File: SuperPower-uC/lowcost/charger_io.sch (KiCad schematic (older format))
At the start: 13 parts, among them J3 USB_C_Receptacle_USB2.0, J4 Solar in, Q3 S8050, Q4 S8050, U5 CH340G, U6 AMS1117-3.3, Y1 12MHZ

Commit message: updated with kicad v5.1.7
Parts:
- J3: footprint Connector_USB:USB_C_Receptacle_XKB_U262-16XN-4BVC11 -> (none)
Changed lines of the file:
@@
 	5250 2900 5250 3100
 Connection ~ 5250 2900
-Connection ~ 4700 3150
 Wire Wire Line
 	4700 3150 4900 3150
 Wire Wire Line
 	4700 3250 4700 3150
-Connection ~ 4700 3450
 Wire Wire Line
 	4700 3450 4700 3350
 Wire Wire Line
 	4700 3450 5000 3450
-$Comp
-L Connector:USB_C_Receptacle_USB2.0 J3
-U 1 1 5F7DCB22
-P 4100 3250
-F 0 "J3" H 4207 4117 50  0000 C CNN
-F 1 "USB_C_Receptacle_USB2.0" H 4207 4026 50  0000 C CNN
-F 2 "Connector_USB:USB_C_Receptacle_XKB_U262-16XN-4BVC11" H 4250 3250 50  0001 C CNN
-F 3 "https://datasheet.lcsc.com/szlcsc/2002271811_XKB-Connectivity-U262-161N-4BVC11_C319148.pdf" H 4250 3250 50  0001 C CNN
-	1    4100 3250
-	1    0    0    -1
-$EndComp
 Wire Wire Line
 	6350 2600 6350 2750
@@
 Text HLabel 6700 2600 2    50   Output ~ 0
 VCHARGE
+$Comp
+L Connector:USB_C_Receptacle_USB2.0 J3
+U 1 1 5F80E438
+P 4100 3250
+F 0 "J3" H 4207 4117 50  0000 C CNN
+F 1 "USB_C_Receptacle_USB2.0" H 4207 4026 50  0000 C CNN
+F 2 "" H 4250 3250 50  0001 C CNN
+F 3 "https://www.usb.org/sites/default/files/documents/usb_type-c.zip" H 4250 3250 50  0001 C CNN
+	1    4100 3250
+	1    0    0    -1
+$EndComp
+Connection ~ 4700 3150
+Connection ~ 4700 3450
 $EndSCHEMATC

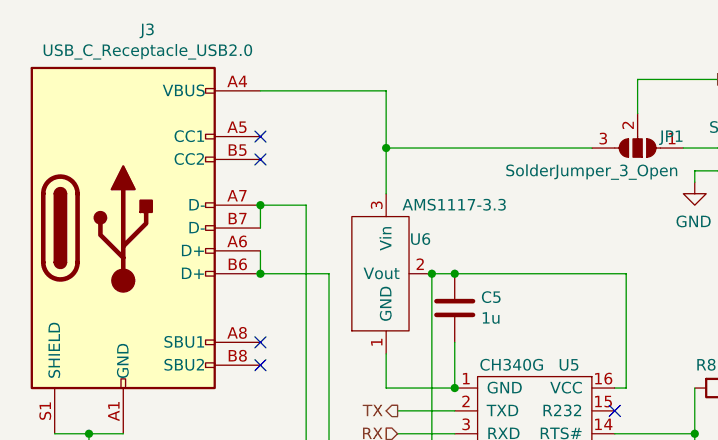
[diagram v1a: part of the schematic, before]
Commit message: added usb cc pin pulldowns and deleted cache
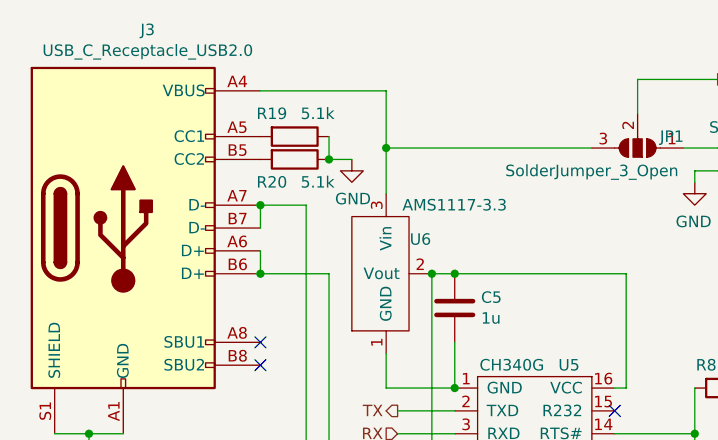
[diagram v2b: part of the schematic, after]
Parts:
- added R19, R20: 5.1k, Resistor_SMD:R_0603_1608Metric_Pad1.05x0.95mm_HandSolder, symbol Device:R
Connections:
- net GND: now also R19.1, R20.1
- net at J3.A5 (CC1): now also R19.2
- net at J3.B5 (CC2): now also R20.2
- no-connect marks 9 -> 7
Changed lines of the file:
@@
 NoConn ~ 4700 3750
 NoConn ~ 4700 3850
-NoConn ~ 4700 2950
-NoConn ~ 4700 2850
 Wire Wire Line
 	5250 2900 5250 3100
@@
 Connection ~ 4700 3150
 Connection ~ 4700 3450
+$Comp
+L Device:R R19
+U 1 1 5F81A493
+P 4850 2850
+F 0 "R19" V 4750 2750 50  0000 C CNN
+F 1 "5.1k" V 4750 2950 50  0000 C CNN
+F 2 "Resistor_SMD:R_0603_1608Metric_Pad1.05x0.95mm_HandSolder" V 4780 2850 50  0001 C CNN
+F 3 "~" H 4850 2850 50  0001 C CNN
+F 4 "C23186" V 4850 2850 50  0001 C CNN "LCSC"
+	1    4850 2850
+	0    1    1    0
+$EndComp
+$Comp
+L Device:R R20
+U 1 1 5F81C386
+P 4850 2950
+F 0 "R20" V 4950 2850 50  0000 C CNN
+F 1 "5.1k" V 4950 3050 50  0000 C CNN
+F 2 "Resistor_SMD:R_0603_1608Metric_Pad1.05x0.95mm_HandSolder" V 4780 2950 50  0001 C CNN
+F 3 "~" H 4850 2950 50  0001 C CNN
+F 4 "C23186" V 4850 2950 50  0001 C CNN "LCSC"
+	1    4850 2950
+	0    1    1    0
+$EndComp
+Wire Wire Line
+	5000 2850 5000 2950
+$Comp
+L power:GND #PWR?
+U 1 1 5F820F01
+P 5100 2950
+F 0 "#PWR?" H 5100 2700 50  0001 C CNN
+F 1 "GND" H 5105 2777 50  0000 C CNN
+F 2 "" H 5100 2950 50  0001 C CNN
+F 3 "" H 5100 2950 50  0001 C CNN
+	1    5100 2950
+	1    0    0    -1
+$EndComp
+Wire Wire Line
+	5100 2950 5000 2950
+Connection ~ 5000 2950
 $EndSCHEMATC

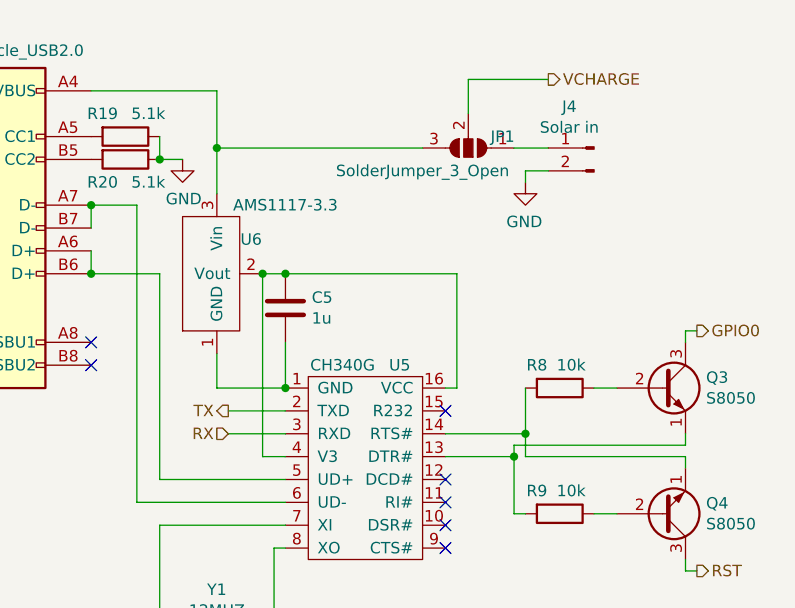
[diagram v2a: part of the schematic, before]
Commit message: fixed erc errors
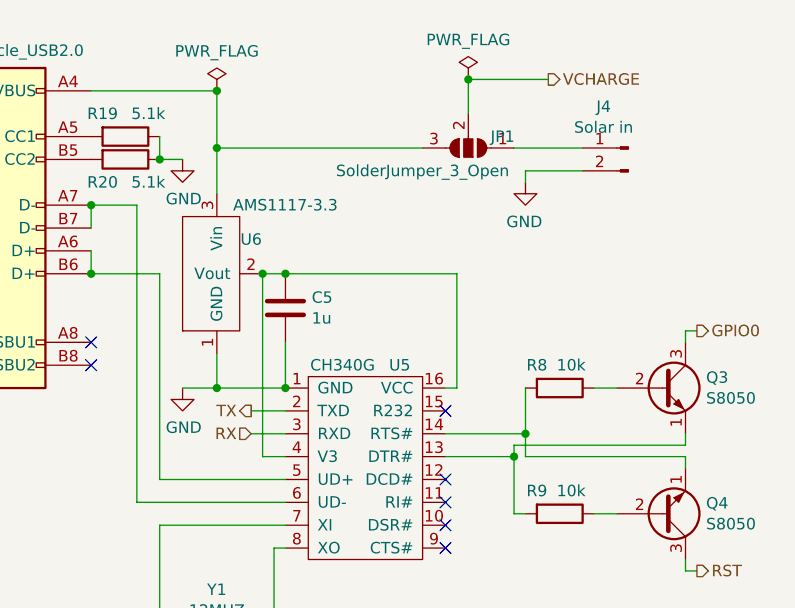
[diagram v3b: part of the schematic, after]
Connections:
- net GND: now also C5.2, U5.1 (GND), U6.1 (GND)
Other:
- moved on the sheet: J4
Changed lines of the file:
@@
 Wire Wire Line
 	5250 2900 6150 2900
-Wire Wire Line
-	6700 2900 6550 2900
 Connection ~ 5000 5100
 Wire Wire Line
@@
 	6600 3000 6600 3050
 Wire Wire Line
-	6700 3000 6600 3000
+	6850 3000 6600 3000
 $Comp
 L power:GND #PWR0123
@@
 $EndComp
 Wire Wire Line
-	5300 4150 5550 4150
-Wire Wire Line
-	5300 4050 5550 4050
+	5400 4150 5550 4150
+Wire Wire Line
+	5400 4050 5550 4050
 Connection ~ 5550 3950
 Wire Wire Line
@@
 L Connector:Conn_01x02_Male J4
 U 1 1 5F7CE401
-P 6900 2900
-F 0 "J4" H 7008 3081 50  0000 C CNN
-F 1 "Solar in" H 7008 2990 50  0000 C CNN
-F 2 "Connector_JST:JST_EH_S2B-EH_1x02_P2.50mm_Horizontal" H 6900 2900 50  0001 C CNN
-F 3 "https://datasheet.lcsc.com/szlcsc/1811051822_JST-Sales-America-S2B-XH-A-LF-SN_C157931.pdf" H 6900 2900 50  0001 C CNN
-F 4 "C157931" H 6900 2900 50  0001 C CNN "LCSC"
-	1    6900 2900
+P 7050 2900
+F 0 "J4" H 7158 3081 50  0000 C CNN
+F 1 "Solar in" H 7158 2990 50  0000 C CNN
+F 2 "Connector_JST:JST_EH_S2B-EH_1x02_P2.50mm_Horizontal" H 7050 2900 50  0001 C CNN
+F 3 "https://datasheet.lcsc.com/szlcsc/1811051822_JST-Sales-America-S2B-XH-A-LF-SN_C157931.pdf" H 7050 2900 50  0001 C CNN
+F 4 "C157931" H 7050 2900 50  0001 C CNN "LCSC"
+	1    7050 2900
 	-1   0    0    -1
 $EndComp
@@
 	1    0    0    -1
 $EndComp
-Text HLabel 5300 4150 0    50   Input ~ 0
+Text HLabel 5400 4150 0    50   Input ~ 0
 RX
-Text HLabel 5300 4050 0    50   Output ~ 0
+Text HLabel 5400 4050 0    50   Output ~ 0
 TX
 Text HLabel 6700 2600 2    50   Output ~ 0
@@
 	5000 2850 5000 2950
 $Comp
-L power:GND #PWR?
+L power:GND #PWR0124
 U 1 1 5F820F01
 P 5100 2950
-F 0 "#PWR?" H 5100 2700 50  0001 C CNN
+F 0 "#PWR0124" H 5100 2700 50  0001 C CNN
 F 1 "GND" H 5105 2777 50  0000 C CNN
 F 2 "" H 5100 2950 50  0001 C CNN
@@
 	5100 2950 5000 2950
 Connection ~ 5000 2950
+$Comp
+L power:GND #PWR0125
+U 1 1 5F8616D9
+P 5100 3950
+F 0 "#PWR0125" H 5100 3700 50  0001 C CNN
+F 1 "GND" H 5105 3777 50  0000 C CNN
+F 2 "" H 5100 3950 50  0001 C CNN
+F 3 "" H 5100 3950 50  0001 C CNN
+	1    5100 3950
+	1    0    0    -1
+$EndComp
+Wire Wire Line
+	5100 3950 5250 3950
+Connection ~ 5250 3950
+$Comp
+L power:PWR_FLAG #FLG0101
+U 1 1 5F872CCA
+P 5250 2650
+F 0 "#FLG0101" H 5250 2725 50  0001 C CNN
+F 1 "PWR_FLAG" H 5250 2823 50  0000 C CNN
+F 2 "" H 5250 2650 50  0001 C CNN
+F 3 "~" H 5250 2650 50  0001 C CNN
+	1    5250 2650
+	1    0    0    -1
+$EndComp
+Connection ~ 5250 2650
+$Comp
+L power:PWR_FLAG #FLG0104
+U 1 1 5F8735A3
+P 6350 2600
+F 0 "#FLG0104" H 6350 2675 50  0001 C CNN
+F 1 "PWR_FLAG" H 6350 2773 50  0000 C CNN
+F 2 "" H 6350 2600 50  0001 C CNN
+F 3 "~" H 6350 2600 50  0001 C CNN
+	1    6350 2600
+	1    0    0    -1
+$EndComp
+Connection ~ 6350 2600
+Wire Wire Line
+	6550 2900 6850 2900
 $EndSCHEMATC

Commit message: design rule optimisation
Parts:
- added C21: 1µF, Capacitor_SMD:C_0603_1608Metric_Pad1.05x0.95mm_HandSolder, symbol Device:C
- C5: value 1u -> 1µF
- C6, C7: value 22p -> 22pF
- JP1: value SolderJumper_3_Open -> CHRG_Jumper
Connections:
- net GND: now also C5.1, C21.2; no longer C5.2, J3.S1 (SHIELD)
- net 3v3FTDI: now reaches U5.16 (VCC), U5.4 (V3), U6.2 (Vout)
- net 3v3FTDI: now also C5.2; no longer C5.1
- net D+: now reaches J3.A6 (D+), J3.B6 (D+), U5.5 (UD+)
- net D-: now reaches J3.A7 (D-), J3.B7 (D-), U5.6 (UD-)
- net VBUS: now reaches J3.A4 (VBUS), J3.A9 (VBUS), J3.B4 (VBUS), J3.B9 (VBUS), JP1.3 (B), U6.3 (Vin)
- net VBUS: now also C21.1
- no-connect marks 7 -> 8
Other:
- moved on the sheet: C5, C6, C7, J4, JP1, Q3, Q4, R8, R9, U6, Y1

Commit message: schematic layout cleaning
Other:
- note added: "FTDI supply\n"
- note added: "FTDI\n"
- note added: "Labels\n"
- note added: "USB C Input\n"
- moved on the sheet: C21, C5, C6, C7, J3, J4, JP1, Q3, Q4, R19, R20, R8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

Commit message: swapped led and added usb c part number
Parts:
- J3: LCSC (none) -> C319148
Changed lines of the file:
@@
 F 2 "" H 3150 3600 50  0001 C CNN
 F 3 "https://www.usb.org/sites/default/files/documents/usb_type-c.zip" H 3150 3600 50  0001 C CNN
+F 4 "C319148" H 3000 3600 50  0001 C CNN "LCSC"
 	1    3000 3600
 	1    0    0    -1

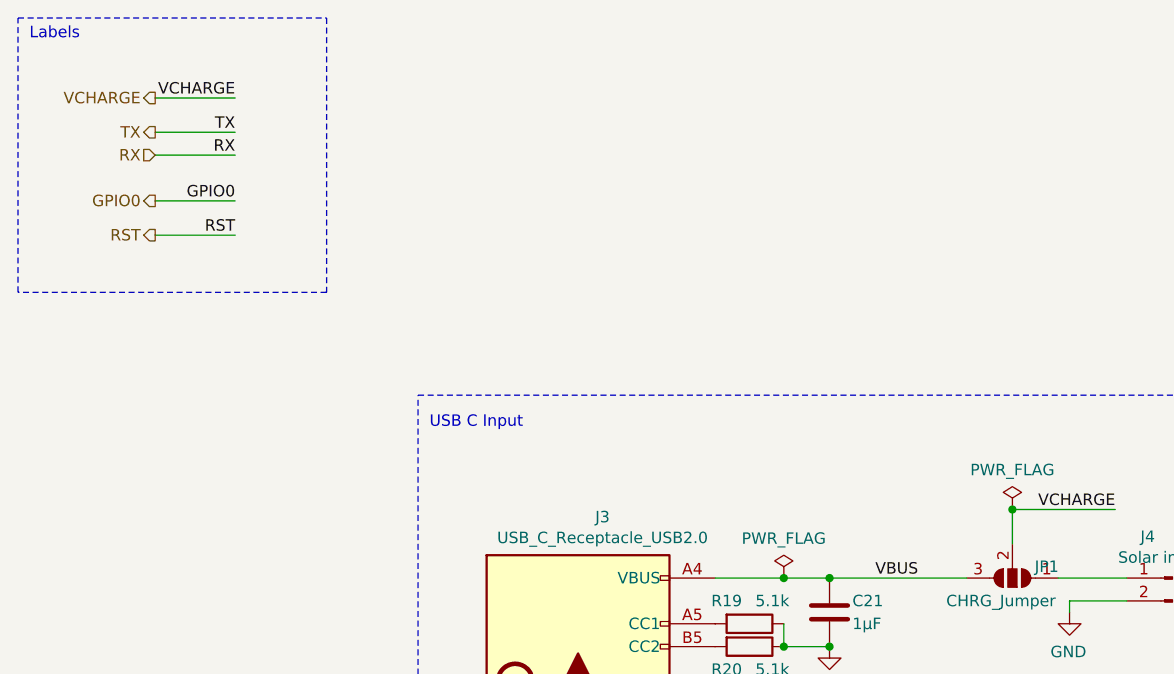
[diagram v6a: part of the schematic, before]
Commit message: modified pin headers to fit devkit version
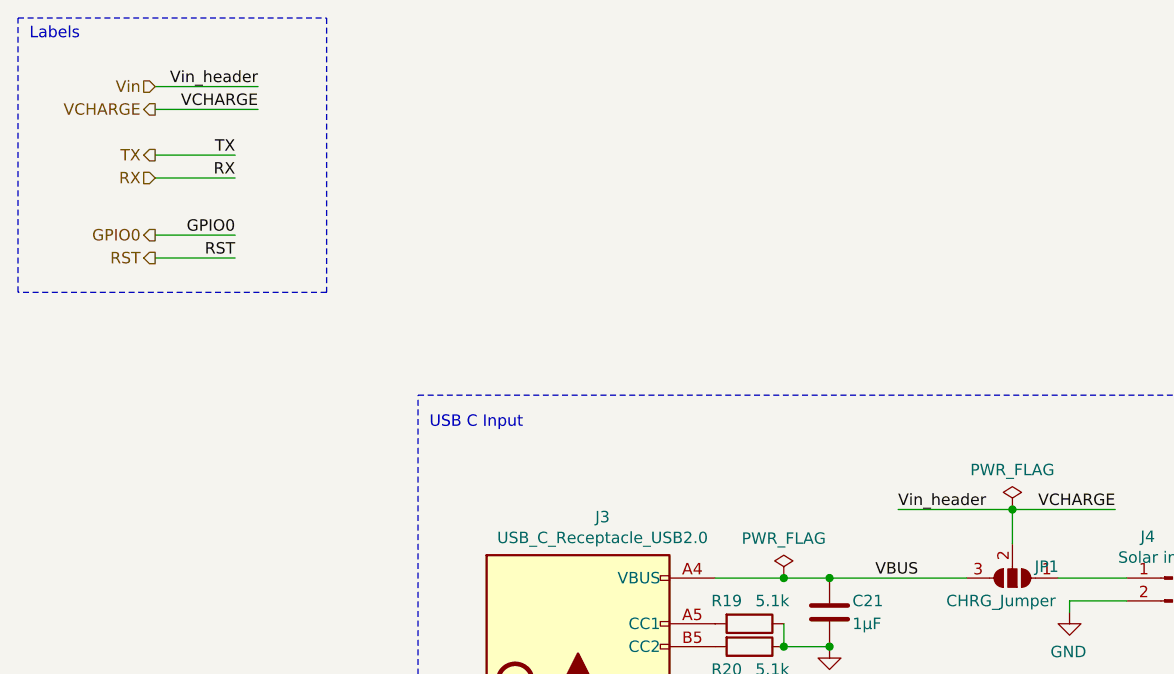
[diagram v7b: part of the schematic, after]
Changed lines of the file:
@@
 $Descr A4 11693 8268
 encoding utf-8
-Sheet 7 7
+Sheet 6 7
 Title "SuperPower-uC"
 Date "2020-09-20"
@@
 Text Notes 2350 2350 0    50   ~ 0
 USB C Input\n
-Text HLabel 1150 900  0    50   Output ~ 0
+Text HLabel 1150 950  0    50   Output ~ 0
 VCHARGE
-Text HLabel 1150 1150 0    50   Input ~ 0
+Text HLabel 1150 1250 0    50   Input ~ 0
 RX
-Text HLabel 1150 1050 0    50   Output ~ 0
+Text HLabel 1150 1150 0    50   Output ~ 0
 TX
-Text HLabel 1150 1350 0    50   Output ~ 0
+Text HLabel 1150 1500 0    50   Output ~ 0
 GPIO0
-Text HLabel 1150 1500 0    50   Output ~ 0
+Text HLabel 1150 1600 0    50   Output ~ 0
 RST
 Wire Wire Line
-	1150 900  1500 900
-Wire Wire Line
-	1150 1050 1500 1050
-Wire Wire Line
-	1500 1350 1150 1350
+	1150 950  1600 950
 Wire Wire Line
 	1150 1150 1500 1150
 Wire Wire Line
 	1500 1500 1150 1500
-Text Label 1500 900  2    50   ~ 0
+Wire Wire Line
+	1150 1250 1500 1250
+Wire Wire Line
+	1500 1600 1150 1600
+Text Label 1600 950  2    50   ~ 0
 VCHARGE
-Text Label 1500 1050 2    50   ~ 0
+Text Label 1500 1150 2    50   ~ 0
 TX
-Text Label 1500 1150 2    50   ~ 0
+Text Label 1500 1250 2    50   ~ 0
 RX
-Text Label 1500 1350 2    50   ~ 0
+Text Label 1500 1500 2    50   ~ 0
 GPIO0
-Text Label 1500 1500 2    50   ~ 0
+Text Label 1500 1600 2    50   ~ 0
 RST
 Text Label 9450 3500 2    50   ~ 0
@@
 Text Notes 600  650  0    50   ~ 0
 Labels\n
+Text HLabel 1150 850  0    50   Input ~ 0
+Vin
+Wire Wire Line
+	1150 850  1600 850
+Text Label 1600 850  2    50   ~ 0
+Vin_header
+Text Label 4400 2700 0    50   ~ 0
+Vin_header
+Wire Wire Line
+	4400 2700 4900 2700
 $EndSCHEMATC

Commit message: started pcb and added missing net labels
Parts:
- J3: footprint (none) -> Connector_USB:USB_C_Receptacle_Palconn_UTC16-G
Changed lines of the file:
@@
 F 0 "J3" H 3107 4467 50  0000 C CNN
 F 1 "USB_C_Receptacle_USB2.0" H 3107 4376 50  0000 C CNN
-F 2 "" H 3150 3600 50  0001 C CNN
+F 2 "Connector_USB:USB_C_Receptacle_Palconn_UTC16-G" H 3150 3600 50  0001 C CNN
 F 3 "https://www.usb.org/sites/default/files/documents/usb_type-c.zip" H 3150 3600 50  0001 C CNN
 F 4 "C319148" H 3000 3600 50  0001 C CNN "LCSC"
